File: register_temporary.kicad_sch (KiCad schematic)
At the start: 11 parts, among them U102 74LS00, U61 74LS161, U62 74LS02

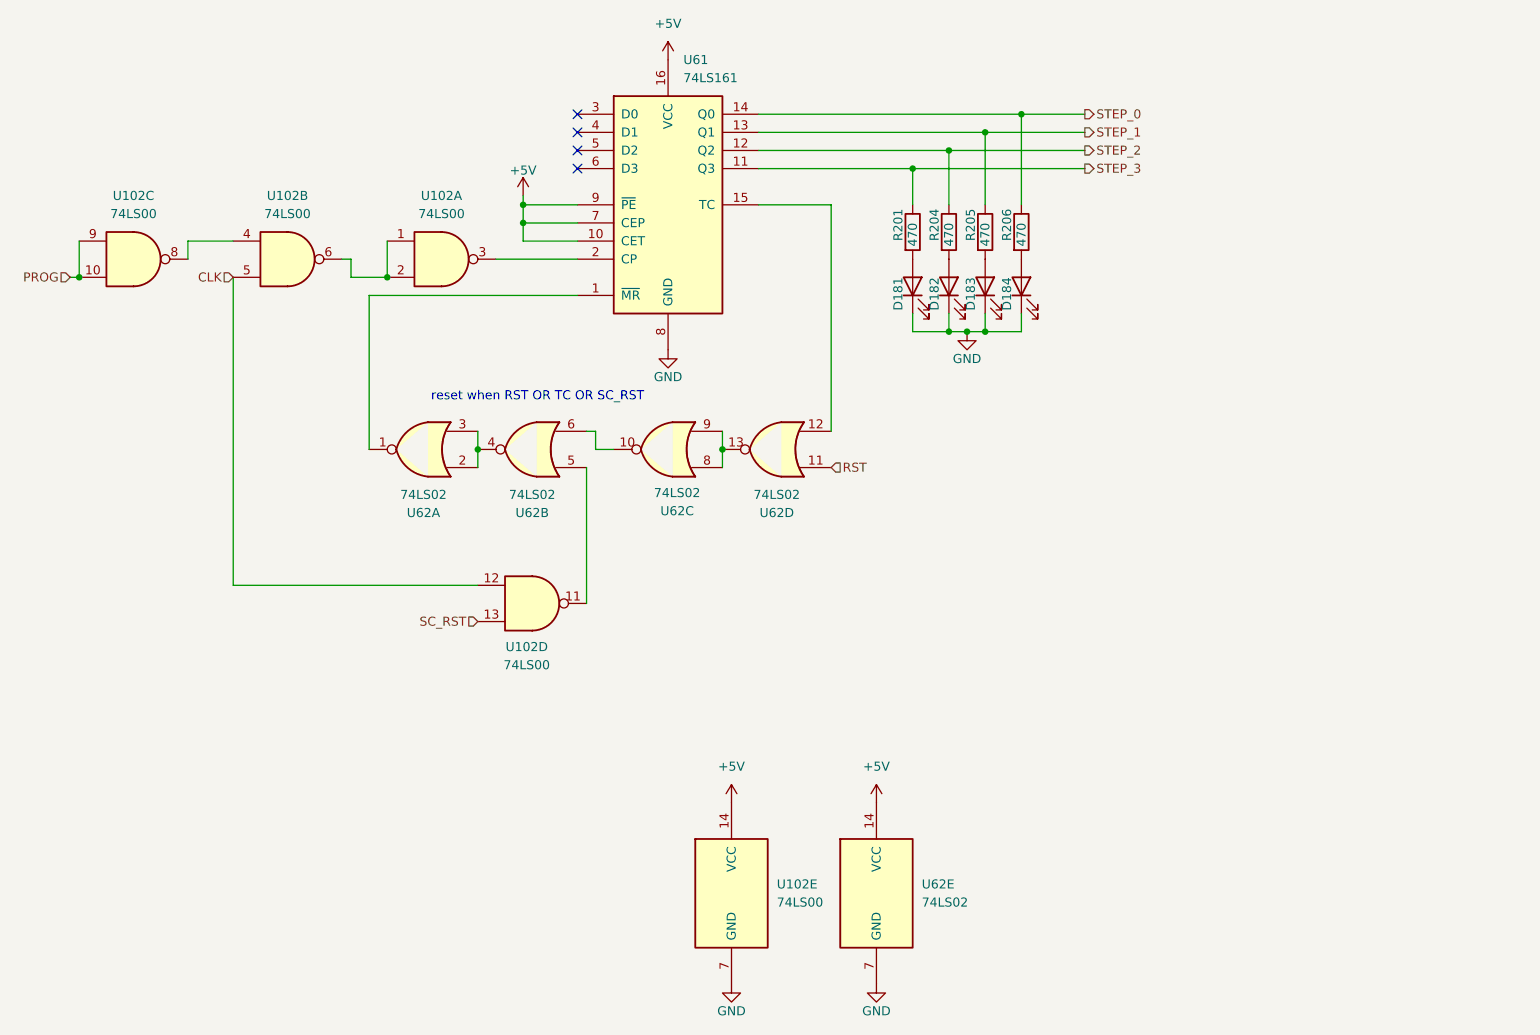
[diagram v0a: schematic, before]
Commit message: chore: sync design between simulation and schematic
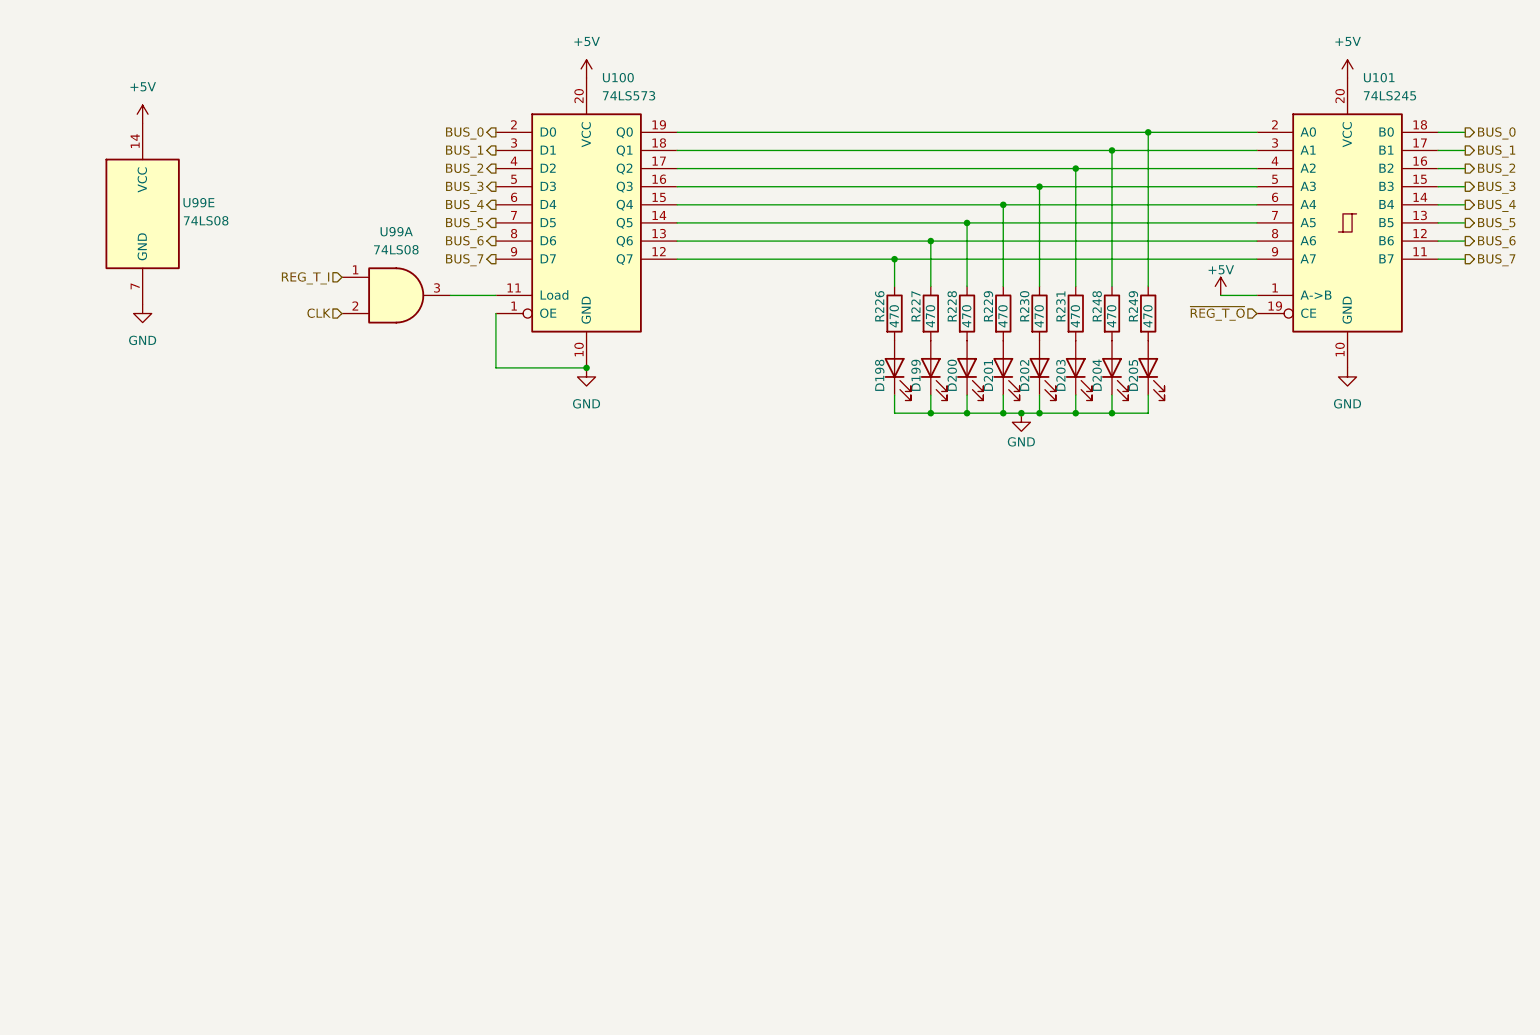
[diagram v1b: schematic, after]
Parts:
- removed D181, D182, D183, D184: LED, LED_SMD:LED_0805_2012Metric, symbol Device:LED
- removed R201, R204, R205, R206: 470, Resistor_SMD:R_0805_2012Metric, symbol Device:R
- removed U102: 74LS00, symbol 74xx:74LS00
- removed U61: 74LS161, Package_DIP:DIP-16_W7.62mm_Socket, symbol 74xx:74LS161
- removed U62: 74LS02, Package_DIP:DIP-14_W7.62mm_Socket, symbol 74xx:74LS02
- added D198, D199, D200, D201, D202, D203, D204, D205: LED, LED_SMD:LED_0805_2012Metric, symbol Device:LED
- added R226, R227, R228, R229, R230, R231, R248, R249: 470, Resistor_SMD:R_0805_2012Metric, symbol Device:R
- added U100: 74LS573, Package_DIP:DIP-20_W7.62mm_Socket, symbol 74xx:74LS573
- added U101: 74LS245, Package_DIP:DIP-20_W7.62mm_Socket, symbol 74xx:74LS245
- added U99: 74LS08, Package_DIP:DIP-14_W7.62mm_Socket, symbol 74xx:74LS08
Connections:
- net +5V: now also U100.20 (VCC), U101.1 (A->B), U101.20 (VCC), U99.14 (VCC)
- net CLK: now also U99.2
- net GND: now also D198.1 (K), D199.1 (K), D200.1 (K), D201.1 (K), D202.1 (K), D203.1 (K), D204.1 (K), D205.1 (K), U100.1 (OE), U100.10 (GND), U101.10 (GND), U99.7 (GND)
- new net: R228.1, U100.14 (Q5), U101.7 (A5)
- new net: D200.2 (A), R228.2
- new net: U100.11 (Load), U99.3
- new net: R226.1, U100.12 (Q7), U101.9 (A7)
- new net: D198.2 (A), R226.2
- new net: D204.2 (A), R248.2
- new net: R231.1, U100.17 (Q2), U101.4 (A2)
- new net: D203.2 (A), R231.2
- new net: R230.1, U100.16 (Q3), U101.5 (A3)
- new net: D202.2 (A), R230.2
- new net: D199.2 (A), R227.2
- new net: R248.1, U100.18 (Q1), U101.3 (A1)
- new net: R249.1, U100.19 (Q0), U101.2 (A0)
- new net: D205.2 (A), R249.2
- new net: D201.2 (A), R229.2
- new net: R227.1, U100.13 (Q6), U101.8 (A6)
- new net: R229.1, U100.15 (Q4), U101.6 (A4)
- new net BUS_0: U100.2 (D0), U101.18 (B0)
- new net BUS_1: U100.3 (D1), U101.17 (B1)
- new net BUS_2: U100.4 (D2), U101.16 (B2)
- new net BUS_3: U100.5 (D3), U101.15 (B3)
- new net BUS_4: U100.6 (D4), U101.14 (B4)
- new net BUS_5: U100.7 (D5), U101.13 (B5)
- new net BUS_6: U100.8 (D6), U101.12 (B6)
- new net BUS_7: U100.9 (D7), U101.11 (B7)
- new net REG_T_I: U99.1
- new net ~{REG_T_O}: U101.19 (CE)
- no-connect marks 4 -> 0
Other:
- note removed: "reset when RST OR TC OR SC_RST"
